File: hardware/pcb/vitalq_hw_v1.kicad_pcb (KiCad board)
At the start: 2 copper layers, 287.4 x 127.5 mm, 155 parts, among them J1 FSR402, J2 USB-C, J3 JST_PH_B2B, J4 EDA, J5 ECG, J6 AFE_ECG, Q1 AO3401A, Q2 BSS138, Q3 MMBT3904, Q4 MMBT3904, SW1 PCM12_as_SPST, SW2 EN, SW3 BOOT, U1 ESP32-WROOM-32E-N8R2, U10 MCP73831T-2ACI/OT, U11 XC6206P332MR-G, U12 TPS7A2033PDBVR, U13 AP2112K-3.3TRG1, U14 XC6206P182MR-G, U15 CP2102N-A02-GQFN28R, U16 PCA9306DC, U17 USBLC6-2SC6, U2 AFE4900YZR, U3 AD5940BCBZ, U4 ADS1292RIPBSR, U5 TMP117, U6 AS7341-DLGM, U7 MLX90632SLD-DCB-000-RE, U8 BME280, U9 LSM6DSV80XTR, Y1 16MHz

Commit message: Rebuild the hw_v1 board around the reduced part list.
Replace the stub hierarchy and import-grid PCB with an explicit
seven-sheet schematic and a 52 x 40 mm two-sided wearable placement.
AS7341 stays on a 1.8 V TPS7A2018, with one PCA9306 for its I2C bus.

Co-authored-by: Riyu-D1 <Riyu-D1@users.noreply.github.com>
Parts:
- removed C43: 12pF, C_0603_1608Metric
- removed C44, C46, C48: 10uF, C_0805_2012Metric
- removed C45, C47, C49, C56, C57, C58, C59, C60, C61, C62, C63, C64, C65, C66, C67: 100nF, C_0603_1608Metric
- removed C50, C51: 1uF, C_0603_1608Metric
- removed C52: 47nF, C_0603_1608Metric
- removed C53: 4.7nF, C_0603_1608Metric
- removed C54, C55: 2.2nF, C_0603_1608Metric
- removed D1: CHARGE, LED_0603_1608Metric
- removed D2: LED_GREEN_525nm, LED_1206_3216Metric
- removed D3: LED_IR_940nm, LED_1206_3216Metric
- removed D4: LED_RED_660nm, LED_1206_3216Metric
- removed D5: SS14, D_SMA
- removed D6: PIN_PHOTODIODE, D_SOD-123
- removed D7: AS7341_LED, LED_0603_1608Metric
- removed Q1: AO3401A, SOT-23
- removed Q2: BSS138, SOT-23
- removed Q3, Q4: MMBT3904, SOT-23
- removed R23, R24: 1k, R_0603_1608Metric
- removed R25, R26, R27, R28, R29, R30, R45, R46, R47, R48: 10k, R_0603_1608Metric
- removed R31, R32, R35, R36, R37: 1M, R_0603_1608Metric
- removed R33, R34: 10M, R_0603_1608Metric
- removed R38, R39: 40.2k, R_0603_1608Metric
- removed R40, R41, R42, R43: 4.7k, R_0603_1608Metric
- removed R44: 200, R_0603_1608Metric
- removed R49, R50: 100k, R_0603_1608Metric
- removed SW1: PCM12_as_SPST, SW_SPDT_PCM12
- removed SW2: EN, SW_SPST_TL3342
- removed SW3: BOOT, SW_SPST_TL3342
- removed U15: CP2102N-A02-GQFN28R, QFN-28-1EP_5x5mm_P0.5mm_EP3.35x3.35mm
- removed U16: PCA9306DC, VSSOP-8_2.3x2mm_P0.5mm
- removed U17: USBLC6-2SC6, SOT-23-6
- removed Y1: 16MHz, Crystal_SMD_3215-2Pin_3.2x1.5mm
- added H1: M2, MountingHole:MountingHole_2.2mm_M2, F.Cu at (48.6, 2.80)
- added H2: M2, MountingHole:MountingHole_2.2mm_M2, F.Cu at (9.20, 5.60)
- added TP1: EN, TestPoint:TestPoint_Pad_D1.5mm, F.Cu at (28.6, 19.6)
- added TP2: IO0, TestPoint:TestPoint_Pad_D1.5mm, F.Cu at (28.6, 16.6)
- C1, C2: value 4.7uF -> 4.7u; footprint C_0805_2012Metric -> Capacitor_SMD:C_0402_1005Metric
- C10, C3, C33, C4, C5, C6: value 1uF -> 1u; footprint C_0603_1608Metric -> Capacitor_SMD:C_0402_1005Metric
- C11: value 4.7uF -> 1u; footprint C_0805_2012Metric -> Capacitor_SMD:C_0402_1005Metric; moved to B.Cu
- C12, C17, C24, C25, C27, C37: value 100nF -> 100n; footprint C_0603_1608Metric -> Capacitor_SMD:C_0402_1005Metric; moved to B.Cu
- C13: value 4.7uF -> 100n; footprint C_0805_2012Metric -> Capacitor_SMD:C_0402_1005Metric; moved to B.Cu
- C14: value 100nF -> 1u; footprint C_0603_1608Metric -> Capacitor_SMD:C_0402_1005Metric; moved to B.Cu
- C15, C18, C36: value 1uF -> 100n; footprint C_0603_1608Metric -> Capacitor_SMD:C_0402_1005Metric; moved to B.Cu
- C16: value 10uF -> 1u; footprint C_0805_2012Metric -> Capacitor_SMD:C_0402_1005Metric; moved to B.Cu
- C19, C26: value 1uF -> 1u; footprint C_0603_1608Metric -> Capacitor_SMD:C_0402_1005Metric; moved to B.Cu
- C20: value 4.7uF -> 4.7u; footprint C_0805_2012Metric -> Capacitor_SMD:C_0402_1005Metric; moved to B.Cu
- C21: value 100nF -> 470n; footprint C_0603_1608Metric -> Capacitor_SMD:C_0402_1005Metric; moved to B.Cu
- C22: value 100pF -> 470n; footprint C_0603_1608Metric -> Capacitor_SMD:C_0402_1005Metric; moved to B.Cu
- C23: value 10uF -> 470n; footprint C_0805_2012Metric -> Capacitor_SMD:C_0402_1005Metric; moved to B.Cu
- C28, C8: value 1uF -> 100n; footprint C_0603_1608Metric -> Capacitor_SMD:C_0402_1005Metric
- C29: value 4.7uF -> 100n; footprint C_0805_2012Metric -> Capacitor_SMD:C_0402_1005Metric
- C30: value 470nF -> 10u; footprint C_0603_1608Metric -> Capacitor_SMD:C_0402_1005Metric
- C31: value 470nF -> 100n; footprint C_0603_1608Metric -> Capacitor_SMD:C_0402_1005Metric
- C32: value 470nF -> 1u; footprint C_0603_1608Metric -> Capacitor_SMD:C_0402_1005Metric
- C34, C35: value 100nF -> 4.7n; footprint C_0603_1608Metric -> Capacitor_SMD:C_0402_1005Metric
- C38: value 15nF -> 100n; footprint C_0603_1608Metric -> Capacitor_SMD:C_0402_1005Metric; moved to B.Cu
- C39, C40, C41: value 470nF -> 100n; footprint C_0603_1608Metric -> Capacitor_SMD:C_0402_1005Metric; moved to B.Cu
- C42: value 12pF -> 1u; footprint C_0603_1608Metric -> Capacitor_SMD:C_0402_1005Metric; moved to B.Cu
- C7: value 1uF -> 10u; footprint C_0603_1608Metric -> Capacitor_SMD:C_0402_1005Metric
- C9: value 1uF -> 4.7u; footprint C_0603_1608Metric -> Capacitor_SMD:C_0402_1005Metric
- J1: value FSR402 -> USB-C; footprint PinHeader_1x02_P2.54mm_Vertical -> Connector_USB:USB_C_Receptacle_HRO_TYPE-C-31-M-12
- J2: value USB-C -> LiPo; footprint USB_C_Receptacle_HRO_TYPE-C-31-M-12 -> Connector_JST:JST_PH_S2B-PH-SM4-TB_1x02-1MP_P2.00mm_Horizontal
- J3: value JST_PH_B2B -> FSR402; footprint JST_PH_B2B-PH-K_1x02_P2.00mm_Vertical -> Connector_PinHeader_2.54mm:PinHeader_1x02_P2.54mm_Vertical
- J4: value EDA -> PPG; footprint PinHeader_1x04_P2.54mm_Vertical -> Connector_PinHeader_1.27mm:PinHeader_1x06_P1.27mm_Horizontal; moved to B.Cu
- J5: footprint PinHeader_1x03_P2.54mm_Vertical -> Connector_PinHeader_1.27mm:PinHeader_1x03_P1.27mm_Horizontal
- J6: value AFE_ECG -> EDA; footprint PinHeader_1x03_P2.54mm_Vertical -> Connector_PinHeader_1.27mm:PinHeader_1x04_P1.27mm_Horizontal
- R1, R2: value 100k -> 5.1k; footprint R_0603_1608Metric -> Resistor_SMD:R_0402_1005Metric
- R10, R13: value 10k -> 1k; footprint R_0603_1608Metric -> Resistor_SMD:R_0402_1005Metric; moved to B.Cu
- R11: footprint R_0603_1608Metric -> Resistor_SMD:R_0402_1005Metric; moved to B.Cu
- R12: value 10k -> 10; footprint R_0603_1608Metric -> Resistor_SMD:R_0402_1005Metric; moved to B.Cu
- R14, R3, R4: footprint R_0603_1608Metric -> Resistor_SMD:R_0402_1005Metric
- R15: value 1k -> 1M; footprint R_0603_1608Metric -> Resistor_SMD:R_0402_1005Metric
- R16, R17: value 10k -> 1M; footprint R_0603_1608Metric -> Resistor_SMD:R_0402_1005Metric
- R18: value 10k -> 200; footprint R_0603_1608Metric -> Resistor_SMD:R_0402_1005Metric; moved to B.Cu
- R19: value 10 -> 4.7k; footprint R_0603_1608Metric -> Resistor_SMD:R_0402_1005Metric; moved to B.Cu
- R20: value 1k 0.1% -> 4.7k; footprint R_0603_1608Metric -> Resistor_SMD:R_0402_1005Metric; moved to B.Cu
- R21, R22: value 1k -> 4.7k; footprint R_0603_1608Metric -> Resistor_SMD:R_0402_1005Metric; moved to B.Cu
- R5, R6: value 5.1k 1% -> 10k; footprint R_0603_1608Metric -> Resistor_SMD:R_0402_1005Metric
- R7: value 22.1k -> 10k; footprint R_0603_1608Metric -> Resistor_SMD:R_0402_1005Metric
- R8: value 47.5k -> 10k; footprint R_0603_1608Metric -> Resistor_SMD:R_0402_1005Metric
- R9: value 1k -> 10k; footprint R_0603_1608Metric -> Resistor_SMD:R_0402_1005Metric; moved to B.Cu
- U1: footprint ESP32-WROOM-32E -> RF_Module:ESP32-WROOM-32E
- U10: value MCP73831T-2ACI/OT -> AS7341-DLGM; footprint SOT-23-5 -> Package_LGA:AMS_OLGA-8_2x3.1mm_P0.8mm; moved to B.Cu
- U11: value XC6206P332MR-G -> TMP117AIDRVR; footprint SOT-23 -> Package_SON:WSON-6-1EP_2x2mm_P0.65mm_EP1x1.6mm; moved to B.Cu
- U12: value TPS7A2033PDBVR -> MLX90632SLD-DCB-000-RE; footprint SOT-23-5 -> vitalq:MLX90632; moved to B.Cu
- U13: value AP2112K-3.3TRG1 -> BME280; footprint SOT-23-5 -> Package_LGA:Bosch_LGA-8_2.5x2.5mm_P0.65mm_ClockwisePinNumbering
- U14: value XC6206P182MR-G -> LSM6DSV80XTR; footprint SOT-23 -> vitalq:LSM6DSV80X
- U2: value AFE4900YZR -> MCP73831T-2ACI/OT; footprint AFE4900YZR -> Package_TO_SOT_SMD:SOT-23-5
- U3: value AD5940BCBZ -> XC6206P332MR-G; footprint AD5940BCBZ -> Package_TO_SOT_SMD:SOT-23-3
- U4: value ADS1292RIPBSR -> TPS7A2018PDBVR; footprint TQFP-32_5x5mm_P0.5mm -> Package_TO_SOT_SMD:SOT-23-5
- U5: value TMP117 -> CP2102N-A02-GQFN28R; footprint WSON-6-1EP_2x2mm_P0.65mm_EP1x1.6mm -> Package_DFN_QFN:QFN-28-1EP_5x5mm_P0.5mm_EP3.35x3.35mm
- U6: value AS7341-DLGM -> AFE4900YZR; footprint AMS_OLGA-8_2x3.1mm_P0.8mm -> vitalq:AFE4900YZR; moved to B.Cu
- U7: value MLX90632SLD-DCB-000-RE -> AD5940BCBZ; footprint MLX90632 -> vitalq:AD5940BCBZ
- U8: value BME280 -> ADS1292RIPBSR; footprint Bosch_LGA-8_2.5x2.5mm_P0.65mm_ClockwisePinNumbering -> Package_QFP:TQFP-32_5x5mm_P0.5mm
- U9: value LSM6DSV80XTR -> PCA9306DCUR; footprint LSM6DSV80X -> Package_SO:VSSOP-8_2.3x2mm_P0.5mm; moved to B.Cu
- moved C7 241.7 mm to (28.6, 29.6)
- moved C39 239.9 mm to (35.4, 28.4), turned to 180 degrees
- moved R14 237.1 mm to (35.6, 17.6)
- moved U14 232.4 mm to (21.6, 36.8)
- moved C38 227.2 mm to (39.8, 30.2), turned to 180 degrees
- moved C37 221.0 mm to (37.6, 30.2), turned to 180 degrees
- moved U13 220.6 mm to (15.2, 36.8)
- moved R13 215.7 mm to (50.2, 14.6), turned to 90 degrees
- moved C36 215.2 mm to (35.4, 30.2), turned to 180 degrees
- moved R12 212.9 mm to (46.0, 12.8), turned to 180 degrees
- moved R10 211.3 mm to (32.2, 33.8), turned to 180 degrees
- moved C35 208.8 mm to (33.4, 17.6)
- moved R11 203.6 mm to (48.2, 12.8), turned to 180 degrees
- moved C34 202.1 mm to (31.2, 17.6)
- moved R1 188.5 mm to (47.6, 27.6)
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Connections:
- C10 pad 1: +1V8 -> VBUS
- C11 pad 1: VBUS -> +3V3
- C12 pad 1: VBUS -> +3V3
- C13 pad 1: VDD_CP2102 -> +3V3
- C14 pad 1: VDD_CP2102 -> VBAT
- C15 pad 1: ESP_EN -> AFE_BG
- C18 pad 1: +3.3VA -> +3V3
- C19 pad 1: +3.3VA -> IOVDD
- C20 pad 1: VSYS -> VREF_1V82
- C21 pad 1: N$8 -> VREF_2V5
- C22 pad 1: N$9 -> VBIAS_CAP
- C23 pad 1: +3.3VA -> DVDD_REG
- C24 pad 1: +3.3VA -> VZERO0
- C25 pad 1: +3.3VA -> VBIAS0
- C26 pad 1: +3.3VA -> AIN4_LPF0
- C27 pad 1: +3.3VA -> RC0_0
- C27 pad 2: GND -> RC0_1
- C28 pad 1: IOVDD_AD5940 -> +3V3
- C29 pad 1: N$21 -> +3V3
- C3 pad 1: VSYS -> VBAT
- C30 pad 1: N$22 -> VREFP
- C31 pad 1: N$23 -> VREFP
- C32 pad 1: N$24 -> VCAP1
- C33 pad 1: N$25 -> VCAP2
- C34 pad 1: N$26 -> PGA1N
- C34 pad 2: GND -> PGA1P
- C35 pad 1: N$27 -> PGA2N
- C35 pad 2: GND -> PGA2P
- C36 pad 1: N$28 -> +1V8
- C37 pad 1: N$29 -> +3V3
- C37 pad 2: N$30 -> GND
- C38 pad 1: EDA_CE -> +3V3
- C38 pad 2: N$34 -> GND
- C39 pad 1: EDA_RE -> +3V3
- C39 pad 2: N$36 -> GND
- C40 pad 1: EDA_SE -> +3V3
- C40 pad 2: N$38 -> GND
- C41 pad 1: EDA_DE -> +3V3
- C41 pad 2: N$40 -> GND
- C42 pad 1: N$41 -> AVDD_REG
- C5 pad 1: VSYS -> +3V3
- C6 pad 1: +3.3VA -> +1V8
- C7 pad 1: VSYS -> +3V3
- C8 pad 1: 3V3_S -> +3V3
- C9 pad 1: 3V3_S -> VDD_CP2102
- J3 pad 1: VBAT -> +3V3
- J3 pad 2: GND -> FSR_ADC
- J4 pad 1: N$34 -> VBAT
- J4 pad 2: N$36 -> TX1
- J4 pad 3: N$38 -> TX2
- J4 pad 4: N$40 -> TX3
- J5 pad 1: N$50 -> IN1P
- J5 pad 2: N$51 -> IN1N
- J5 pad 3: N$53 -> RLDOUT
- J6 pad 1: N$17 -> CE0
- J6 pad 2: N$19 -> RE0
- J6 pad 3: N$20 -> SE0
- R1 pad 1: Q1_GATE -> USB_CC1
- R10 pad 1: +3V3 -> AFE_CLK
- R10 pad 2: ESP_EN -> GND
- R11 pad 2: ESP_IO0 -> AD5940_RESET
- R12 pad 2: CS_AD5940 -> IOVDD
- R13 pad 1: +3V3 -> RCAL0
- R13 pad 2: CS_AFE4900 -> RCAL1
- R14 pad 1: +3.3VA -> +3V3
- R14 pad 2: AFE4900_RESETZ -> ADS1292_PWDN
- R15 pad 1: N$10 -> +3V3
- R15 pad 2: GND -> RLDREF
- R16 pad 1: N$16 -> RLDREF
- R16 pad 2: N$17 -> GND
- R17 pad 1: N$18 -> RLDOUT
- R17 pad 2: N$19 -> RLDINV
- R18 pad 1: N$9 -> +3V3
- R18 pad 2: N$20 -> VREF2
- R19 pad 1: +3.3VA -> +3V3
- R19 pad 2: IOVDD_AD5940 -> I2C_SDA
- R2 pad 1: Q1_GATE -> USB_CC2
- R2 pad 2: VBUS -> GND
- R20 pad 1: N$31 -> +3V3
- R20 pad 2: N$32 -> I2C_SCL
- R21 pad 1: N$33 -> +1V8
- R21 pad 2: EDA_CE -> I2C_SDA_1V8
- R22 pad 1: N$35 -> +1V8
- R22 pad 2: EDA_RE -> I2C_SCL_1V8
- R3 pad 1: N$1 -> CHG_PROG
- R4 pad 1: VBUS -> VDD_CP2102
- R4 pad 2: N$2 -> CP_RST
- R5 pad 1: N$4 -> +3V3
- R5 pad 2: GND -> ESP_EN
- R6 pad 1: N$5 -> +3V3
- R6 pad 2: GND -> ESP_IO0
- R7 pad 1: VBUS -> +3V3
- R7 pad 2: CP2102_VBUS -> CS_AD5940
- R8 pad 1: CP2102_VBUS -> FSR_ADC
- R9 pad 1: VDD_CP2102 -> +3V3
- R9 pad 2: CP2102_RST -> AFE4900_RESETZ
- U1 pad 14: (no net) -> unconnected-(U1-IO12-Pad14)
- U1 pad 17: (no net) -> unconnected-(U1-NC-Pad17)
- U1 pad 18: (no net) -> unconnected-(U1-NC-Pad18)
- U1 pad 19: (no net) -> unconnected-(U1-NC-Pad19)
- U1 pad 20: (no net) -> unconnected-(U1-NC-Pad20)
- U1 pad 21: (no net) -> unconnected-(U1-NC-Pad21)
- U1 pad 22: (no net) -> unconnected-(U1-NC-Pad22)
- U1 pad 24: (no net) -> unconnected-(U1-IO2-Pad24)
- U1 pad 26: CS_ADS1292R -> CS_ADS1292
- U1 pad 27: (no net) -> unconnected-(U1-NC-Pad27)
- U1 pad 32: (no net) -> unconnected-(U1-NC-Pad32)
- U1 pad 34: UART_RX -> ESP_RX
- U1 pad 35: UART_TX -> ESP_TX
- U1 pad 4: FSR_SENSE -> FSR_ADC
- U1 pad 5: VBAT_SENSE -> unconnected-(U1-SENSOR_VN-Pad5)
- U1 pad 7: AS7341_INT -> unconnected-(U1-IO35-Pad7)
- U10 pad 1: N$3 -> +1V8
- U10 pad 2: GND -> I2C_SCL_1V8
- U10 pad 3: VBAT -> GND
- U10 pad 4: VBUS -> unconnected-(U10-LDR-Pad4)
- U10 pad 5: N$1 -> GND
- U11 pad 1: GND -> I2C_SCL
- U11 pad 2: VSYS -> GND
- U11 pad 3: 3V3_S -> GND
- U12 pad 1: VSYS -> I2C_SDA
- U12 pad 2: GND -> +3V3
- U12 pad 3: VSYS -> GND
- U12 pad 4: (no net) -> I2C_SCL
- U12 pad 5: +3.3VA -> GND
- U13 pad 1: VSYS -> GND
- U13 pad 2: GND -> +3V3
- U13 pad 3: VSYS -> I2C_SDA
- U13 pad 4: (no net) -> I2C_SCL
- U13 pad 5: +3V3 -> GND
- U14 pad 2: 3V3_S -> GND
- U14 pad 3: +1V8 -> GND
- U4 pad 1: N$47 -> +3V3
- U4 pad 2: N$46 -> GND
- U4 pad 3: ECG_RA -> +3V3
- U4 pad 4: ECG_LA -> unconnected-(U4-NC-Pad4)
- U4 pad 5: ECG_RA -> +1V8
- U5 pad 1: I2C_SCL -> VDD_CP2102
- U5 pad 2: GND -> VDD_CP2102
- U5 pad 3: TMP117_ALERT -> GND
- U5 pad 4: GND -> USB_DP
- U5 pad 5: 3V3_S -> USB_DM
- U5 pad 6: I2C_SDA -> VDD_CP2102
- U5 pad 7: GND -> VBUS
- U8 pad 1: GND -> PGA1N
- U8 pad 2: 3V3_S -> PGA1P
- U8 pad 3: I2C_SDA -> IN1N
- U8 pad 4: I2C_SCL -> IN1P
- U8 pad 5: GND -> IN1N
- U8 pad 6: 3V3_S -> IN1P
- U8 pad 7: GND -> PGA2N
- U8 pad 8: 3V3_S -> PGA2P
- U9 pad 2: GND -> +1V8
- U9 pad 3: GND -> I2C_SCL_1V8
- U9 pad 4: LSM6_INT1 -> I2C_SDA_1V8
- U9 pad 5: 3V3_S -> I2C_SDA
- U9 pad 6: GND -> I2C_SCL
- U9 pad 7: GND -> VREF2
- U9 pad 8: 3V3_S -> VREF2
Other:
- board size 287.4 x 127.5 mm -> 52 x 40 mm
- copper layers 2 -> 4
- board text added: "ECG"
- board text added: "EDA"
- board text added: "MCU"
- board text added: "PWR"
- board text added: "SKIN"
- board text added: "USB"
- board text removed: "IMPORT GRID, not a layout. Place and route this board yourself."

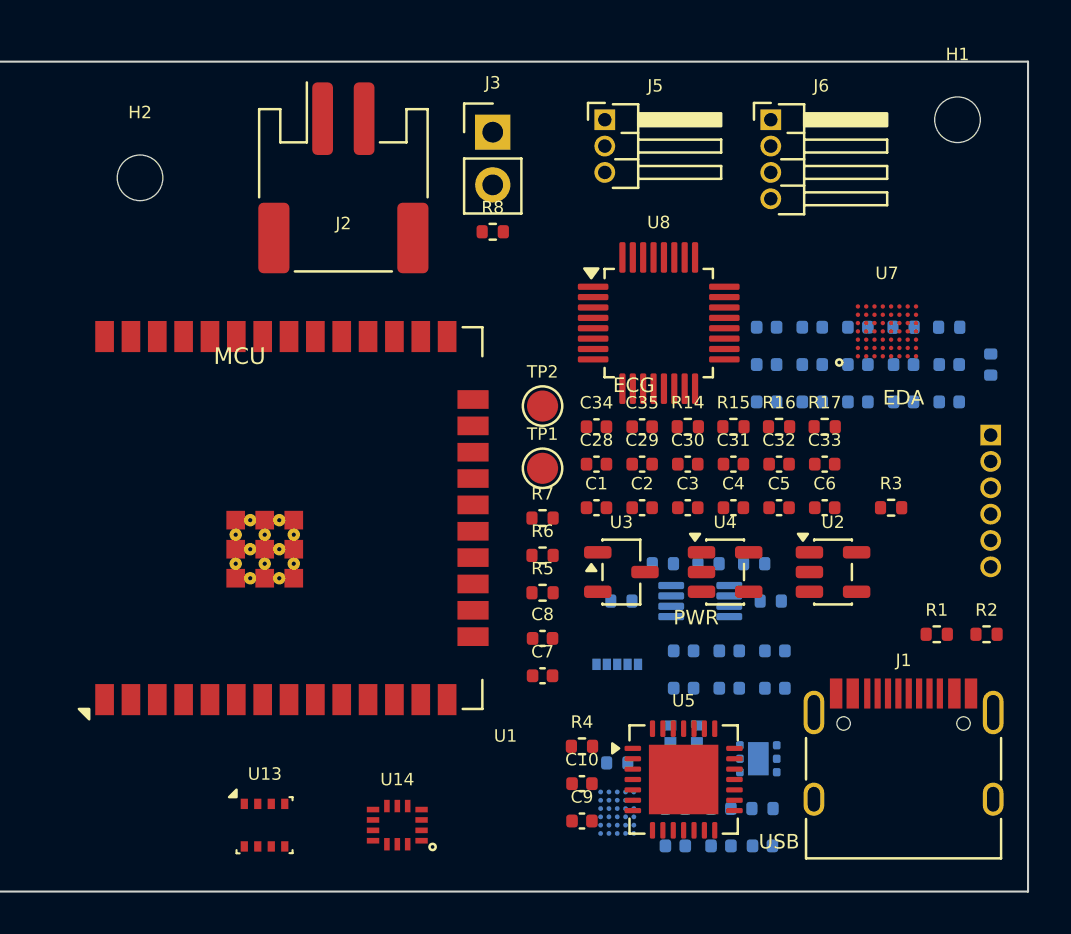
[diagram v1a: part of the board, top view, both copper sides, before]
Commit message: Hide silk designators and separate colliding schematic labels.
Reference and value silk is hidden so 0402 designators no longer overlap pads. The AD5940, AFE4900, and ADS1292 sheets are spaced so net names clear the symbols above them. The part list is unchanged.

Co-authored-by: Riyu-D1 <Riyu-D1@users.noreply.github.com>
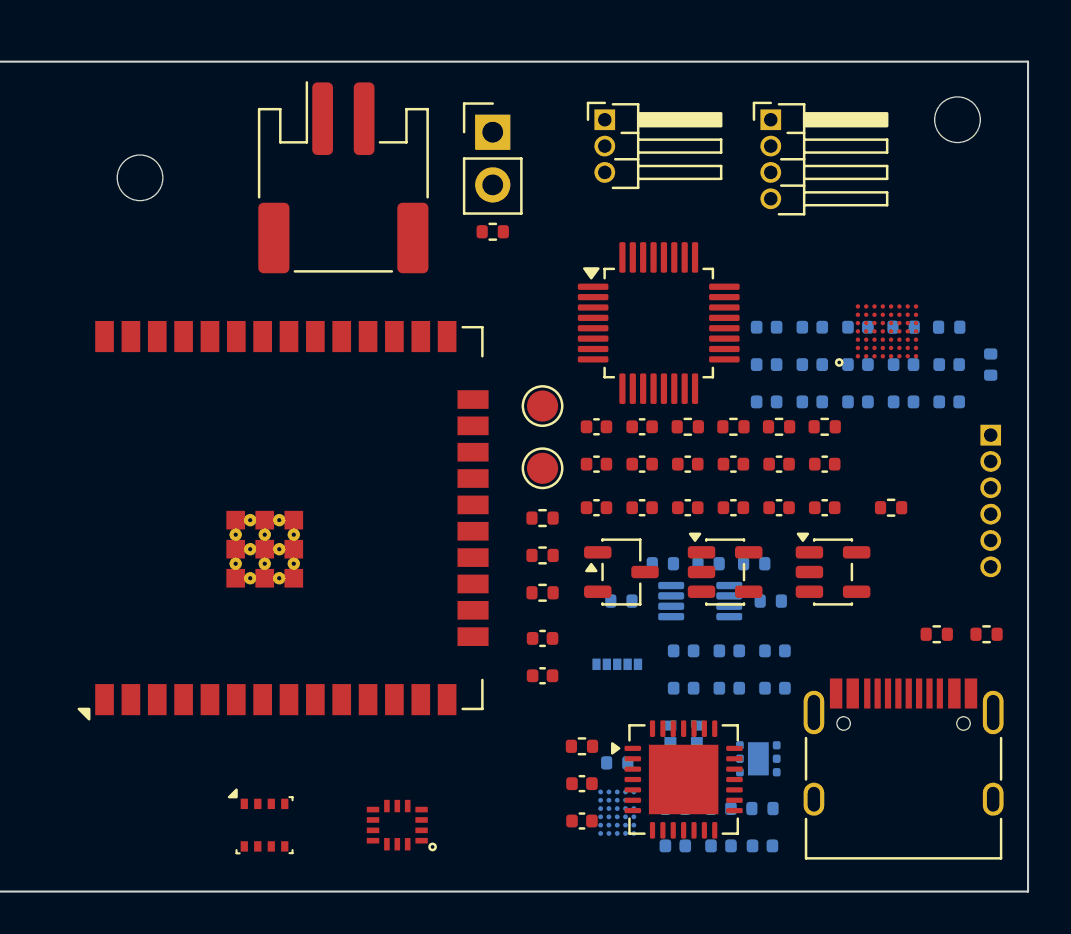
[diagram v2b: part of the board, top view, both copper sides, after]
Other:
- board text removed: "ECG"
- board text removed: "EDA"
- board text removed: "MCU"
- board text removed: "PWR"
- board text removed: "SKIN"
- board text removed: "USB"

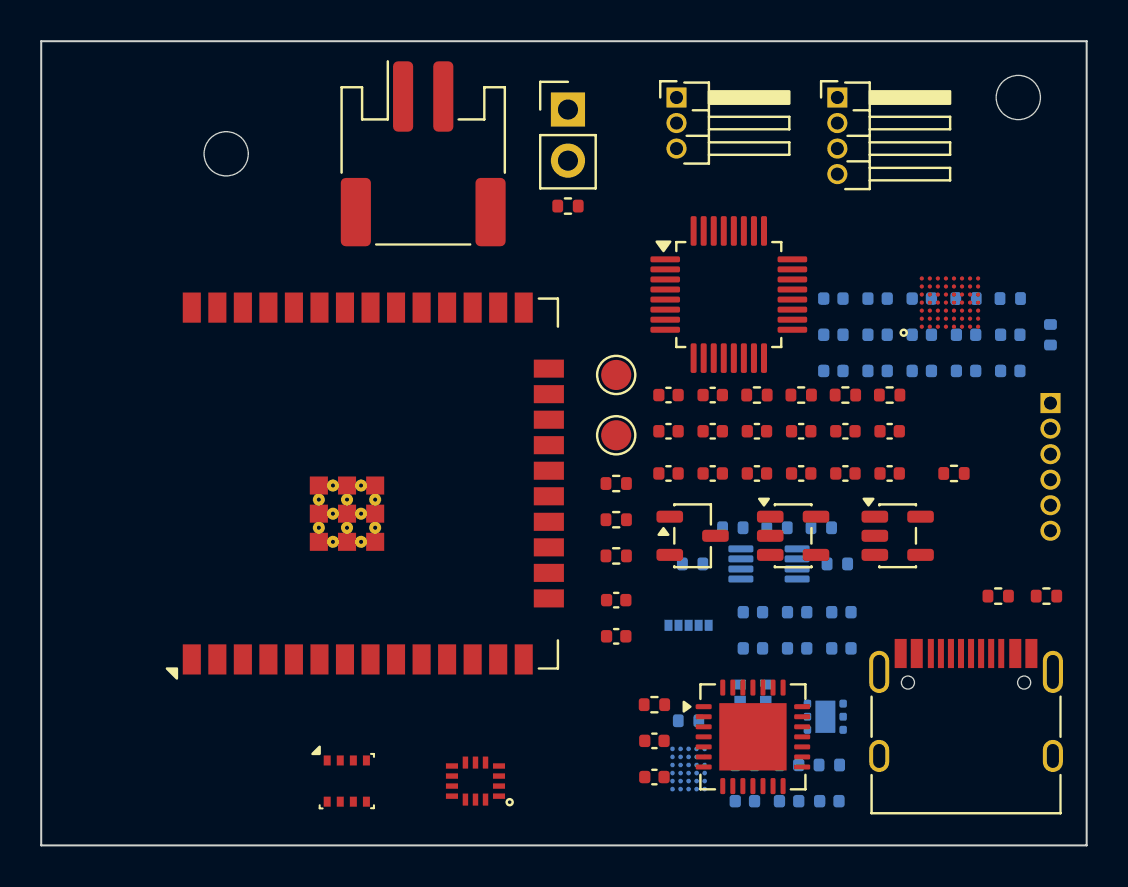
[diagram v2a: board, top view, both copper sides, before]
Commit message: Use official CAD and shrink the hw_v1 board to 37x30 mm.
Replace the hand-drawn AFE4900, AD5940, ADS1292R, AS7341, MLX90632,
TMP117, LSM6DSV80X, and MCP73831 symbols and footprints with the
SnapMagic and Ultra Librarian libraries. ADS1292R is now the QFN-32
ADS1292RIRSMT, and MLX90632SLD-DCB-100-SP moves SDA/SCL onto the
existing 1.8 V bus. Pin headers and mounting holes are flat solder
pads. The unrouted 4-layer placement keeps the antenna on the left
edge and the skin sensors together on the bottom.

Co-authored-by: Riyu-D1 <Riyu-D1@users.noreply.github.com>
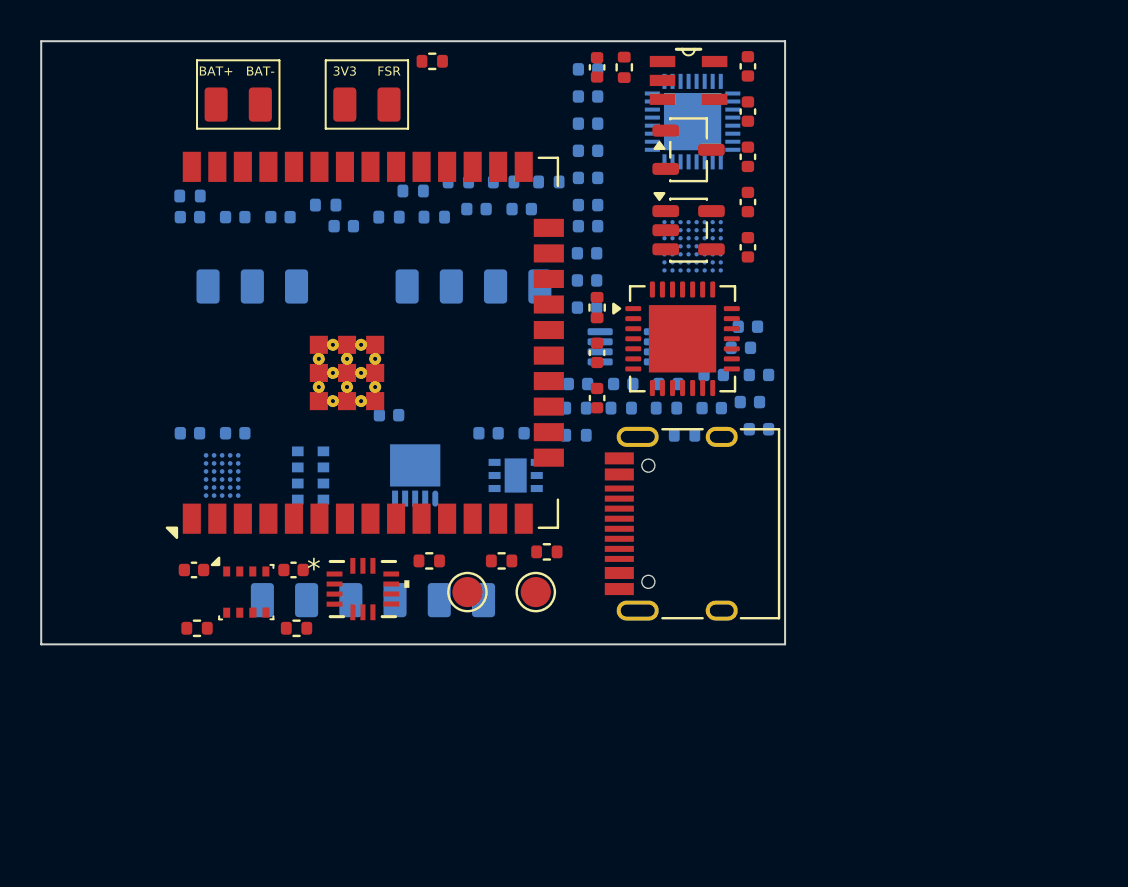
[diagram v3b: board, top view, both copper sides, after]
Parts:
- removed H1, H2: M2, MountingHole:MountingHole_2.2mm_M2
- C28, C29, C30, C31, C32, C33, C34, C35, R14, R15, R16, R17: moved to B.Cu
- J2: value LiPo -> LiPo pads; footprint Connector_JST:JST_PH_S2B-PH-SM4-TB_1x02-1MP_P2.00mm_Horizontal -> vitalq:Pads_LiPo
- J3: value FSR402 -> FSR pads; footprint Connector_PinHeader_2.54mm:PinHeader_1x02_P2.54mm_Vertical -> vitalq:Pads_FSR
- J4: value PPG -> PPG pads; footprint Connector_PinHeader_1.27mm:PinHeader_1x06_P1.27mm_Horizontal -> vitalq:Pads_PPG
- J5: value ECG -> ECG pads; footprint Connector_PinHeader_1.27mm:PinHeader_1x03_P1.27mm_Horizontal -> vitalq:Pads_ECG; moved to B.Cu
- J6: value EDA -> EDA pads; footprint Connector_PinHeader_1.27mm:PinHeader_1x04_P1.27mm_Horizontal -> vitalq:Pads_EDA; moved to B.Cu
- U10: footprint Package_LGA:AMS_OLGA-8_2x3.1mm_P0.8mm -> snap:AS7341DLGT
- U11: footprint Package_SON:WSON-6-1EP_2x2mm_P0.65mm_EP1x1.6mm -> snap:SON65P200X200X80-7N
- U12: value MLX90632SLD-DCB-000-RE -> MLX90632SLD-DCB-100-SP; footprint vitalq:MLX90632 -> snap:MLX90632SLDDCB100SP
- U14: footprint vitalq:LSM6DSV80X -> snap:QFN_LSM6DSV80XTR_STM
- U2: footprint Package_TO_SOT_SMD:SOT-23-5 -> snap:SOT95P280X145-5N
- U6: footprint vitalq:AFE4900YZR -> snap:BGA30N40P5X6_260X210X50
- U7: value AD5940BCBZ -> AD5940BCBZ-RL7; footprint vitalq:AD5940BCBZ -> snap:BGA56C40P8X7_416X356X55; moved to B.Cu
- U8: value ADS1292RIPBSR -> ADS1292RIRSMT; footprint Package_QFP:TQFP-32_5x5mm_P0.5mm -> snap:QFN40P400X400X100-33N-D; moved to B.Cu
- moved R13 43.4 mm to (7.40, 7.70), turned to 180 degrees
- moved R1 39.9 mm to (7.75, 29.2)
- moved C15 39.9 mm to (11.9, 8.75)
- moved C13 38.8 mm to (7.40, 8.75)
- moved C14 38.8 mm to (9.65, 8.75)
- moved R2 37.3 mm to (12.7, 29.2)
- moved J4 35.1 mm to (16.5, 27.8)
- moved R9 35.0 mm to (17.3, 8.75)
- moved C11 34.9 mm to (15.1, 9.20)
- moved R12 32.2 mm to (14.2, 8.15)
- moved C37 32.0 mm to (7.40, 19.5)
- moved C38 32.0 mm to (9.65, 19.5)
- moved C12 30.3 mm to (27.2, 9.20)
- moved R10 28.1 mm to (19.6, 8.75)
- moved U6 27.4 mm to (9.00, 21.6)
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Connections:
- U11 pad 3: GND -> TMP117_ALERT
- U11 pad 4: +3V3 -> GND
- U11 pad 5: TMP117_ALERT -> +3V3
- U12 pad 1: I2C_SDA -> I2C_SDA_1V8
- U12 pad 4: I2C_SCL -> I2C_SCL_1V8
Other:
- board size 52 x 40 mm -> 37 x 30 mm
